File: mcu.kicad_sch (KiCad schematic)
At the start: 7 parts

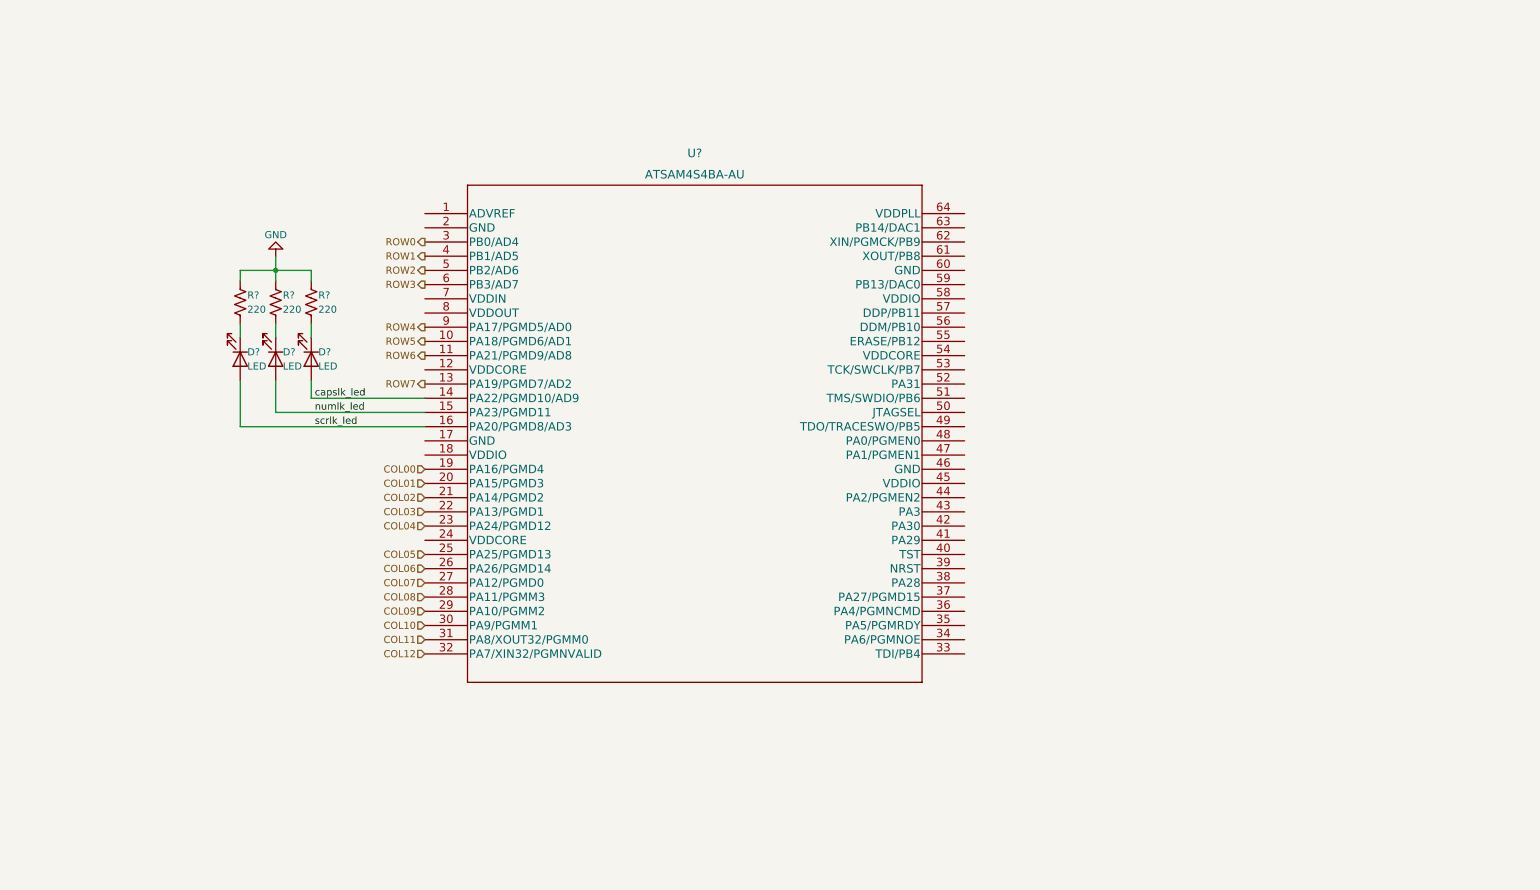
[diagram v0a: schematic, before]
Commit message: Add USB connector and rotary encoder
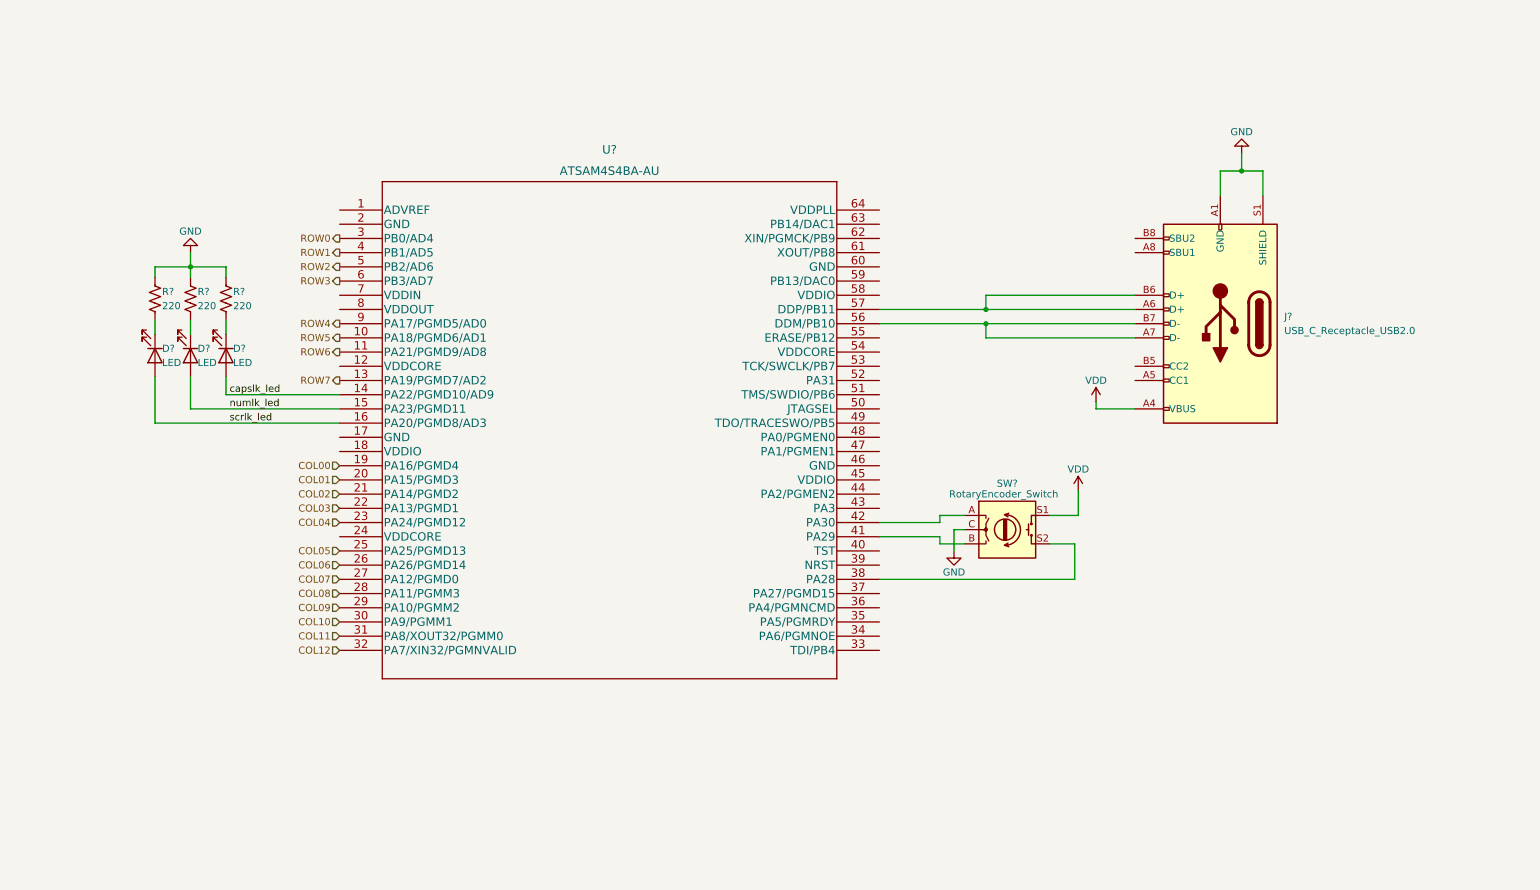
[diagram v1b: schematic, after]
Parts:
- added J?: USB_C_Receptacle_USB2.0, symbol Connector:USB_C_Receptacle_USB2.0
- added SW?: RotaryEncoder_Switch, symbol Device:RotaryEncoder_Switch
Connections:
- net GND: now also J?.A1 (GND), J?.A12 (GND), J?.B1 (GND), J?.B12 (GND), J?.S1 (SHIELD), SW?.C
- net at U?.38 (PA28): now also SW?.S2
- net at U?.41 (PA29): now also SW?.B
- net at U?.42 (PA30): now also SW?.A
- net at U?.56 (DDM/PB10): now also J?.A7 (D-), J?.B7 (D-)
- net at U?.57 (DDP/PB11): now also J?.A6 (D+), J?.B6 (D+)
- new net VDD: J?.A4 (VBUS), J?.A9 (VBUS), J?.B4 (VBUS), J?.B9 (VBUS), SW?.S1
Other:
- moved on the sheet: D?, R?, U?

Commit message: Add vol switches
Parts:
- removed J?: USB_C_Receptacle_USB2.0, symbol Connector:USB_C_Receptacle_USB2.0
- removed SW?: RotaryEncoder_Switch, symbol Device:RotaryEncoder_Switch
- added C?: 2.2u, symbol Device:C
- added C? (x2): 1u, symbol Device:C
- added C? (x2): 22p, symbol Device:C
- added C?: 100n, symbol Device:C
- added C?: 4.7u, symbol Device:C
- added J?: USB_C_Receptacle_USB2.0, symbol Connector:USB_C_Receptacle_USB2.0
- added R? (x2): 56K, symbol Device:R_US
- added R? (x3): 10K, symbol Device:R_US
- added R? (x2): 27, symbol Device:R_US
- added SW? (x3): SW_DIP_x01, symbol Switch:SW_DIP_x01
- added SW?: RotaryEncoder, symbol Device:RotaryEncoder
- added U?: TLV1117LV, symbol LDOs:TLV1117LV
- added Y?: XTAL-12M, symbol Device:Crystal
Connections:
- net GND: now also U?.17 (GND), U?.2 (GND), U?.46 (GND), U?.60 (GND), C?.2, C?.2, C?.2, C?.2, C?.2, C?.2, C?.2, J?.A1 (GND), J?.A12 (GND), J?.B1 (GND), J?.B12 (GND), J?.S1 (SHIELD), R?.1, R?.1, R?.1, R?.1, R?.1, SW?.C, U?.1 (Gnd)
- net VDD: now also U?.1 (ADVREF), U?.18 (VDDIO), U?.45 (VDDIO), U?.58 (VDDIO), U?.7 (VDDIN), C?.1, C?.1, SW?.2, SW?.2, SW?.2, U?.2 (Vout)
- net at U?.42 (PA30): now also SW?.A
- net at U?.41 (PA29): now also SW?.B
- net vol+: now reaches U?.38 (PA28)
- net vol+: now also R?.2, SW?.1
- net vdd_int_reg: now reaches U?.12 (VDDCORE)
- net vdd_int_reg: now also U?.24 (VDDCORE), U?.54 (VDDCORE), U?.64 (VDDPLL), U?.8 (VDDOUT), C?.1, C?.1
- net volm: now reaches U?.36 (PA4/PGMNCMD)
- net volm: now also R?.2, SW?.1
- net vol-: now reaches U?.37 (PA27/PGMD15)
- net vol-: now also R?.2, SW?.1
- net at U?.56 (DDM/PB10): now also R?.1
- net at U?.57 (DDP/PB11): now also R?.1
- net at U?.61 (XOUT/PB8): now also C?.1, Y?.1
- net at U?.62 (XIN/PGMCK/PB9): now also C?.1, Y?.2
- new net: J?.A5 (CC1), R?.2
- new net: J?.B5 (CC2), R?.2
- new net: J?.A6 (D+), J?.B6 (D+), R?.2
- new net: J?.A7 (D-), J?.B7 (D-), R?.2
- new net VBUS: C?.1, J?.A4 (VBUS), J?.A9 (VBUS), J?.B4 (VBUS), J?.B9 (VBUS), U?.3 (Vin)
- no-connect marks 0 -> 2
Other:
- note added: "A 4.7µF or higher ceramic capacitor must be connected between VDDIN and the closest GND pin of the device. This large decoupling capacitor is mandatory to reduce startup current, improving transient response and noise rejection."
- note added: "To ensure stability, an external 2.2 µF output capacitor, CDOUT must be connected between the VDDOUT and the closest GND pin of the device. The ESR of the capacitor must be in the range 0.1 to 10 Ω. Solid tantalum, and multilayer ceramic capacitors are all suitable as output capacitor. A 100 nF bypass capacitor between VDDOUT and the closest GND pin of the device helps decrease output noise and i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"
- moved on the sheet: D?, R?, U?

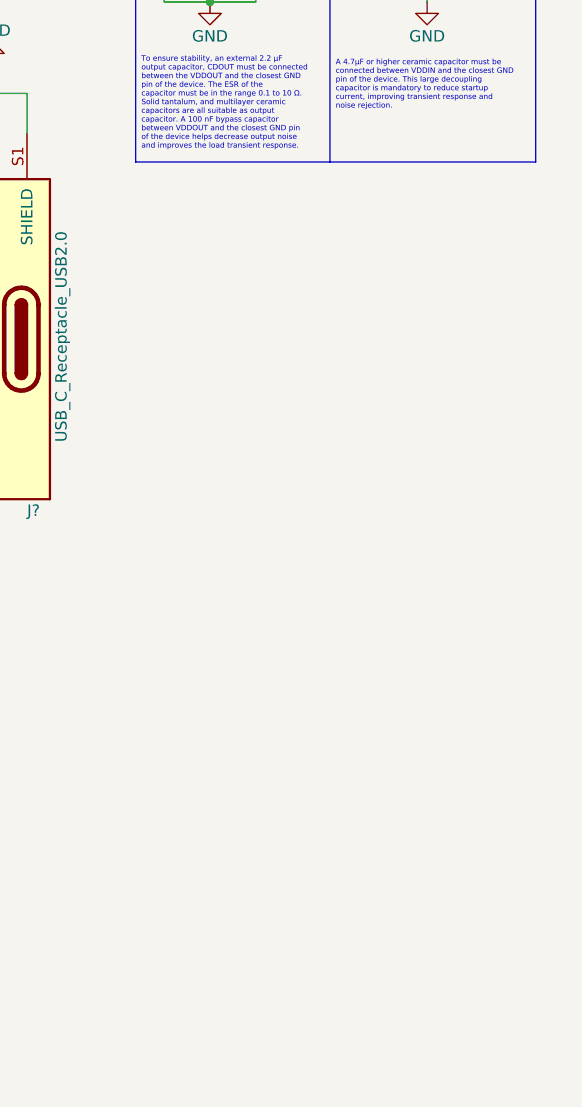
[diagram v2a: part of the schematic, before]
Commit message: Add pulldown resistors to column pins
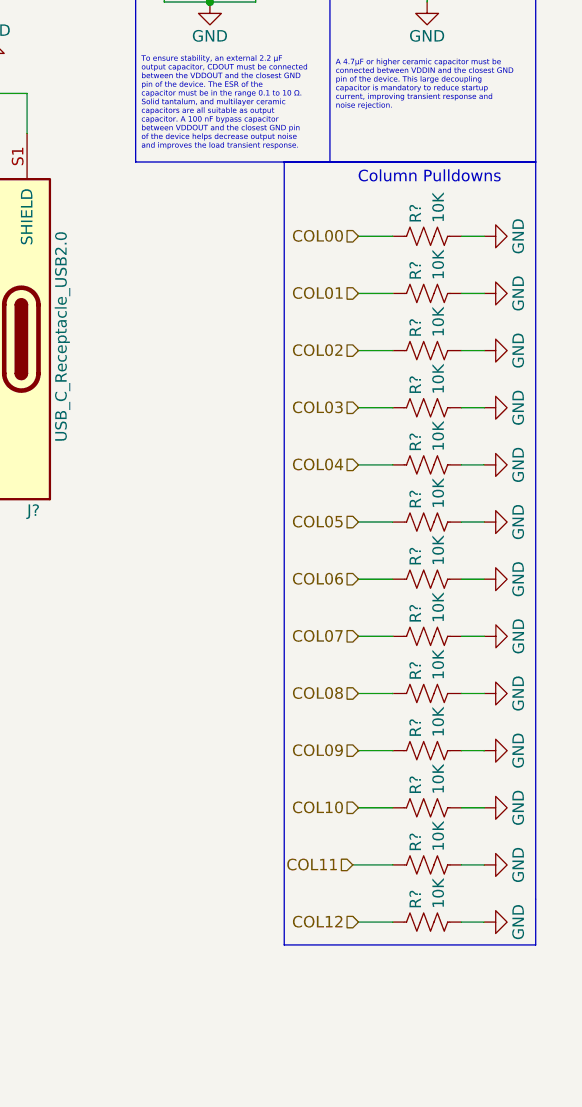
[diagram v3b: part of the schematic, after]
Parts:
- added R? (x13): 10K, symbol Device:R_US
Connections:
- net COL00: now also R?.1
- net COL01: now also R?.1
- net COL02: now also R?.1
- net COL03: now also R?.1
- net COL04: now also R?.1
- net COL05: now also R?.1
- net COL06: now also R?.1
- net COL07: now also R?.1
- net COL08: now also R?.1
- net COL09: now also R?.1
- net COL10: now also R?.1
- net COL11: now also R?.1
- net COL12: now also R?.1
- net GND: now also R?.2, R?.2, R?.2, R?.2, R?.2, R?.2, R?.2, R?.2, R?.2, R?.2, R?.2, R?.2
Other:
- note added: "Column Pulldowns"

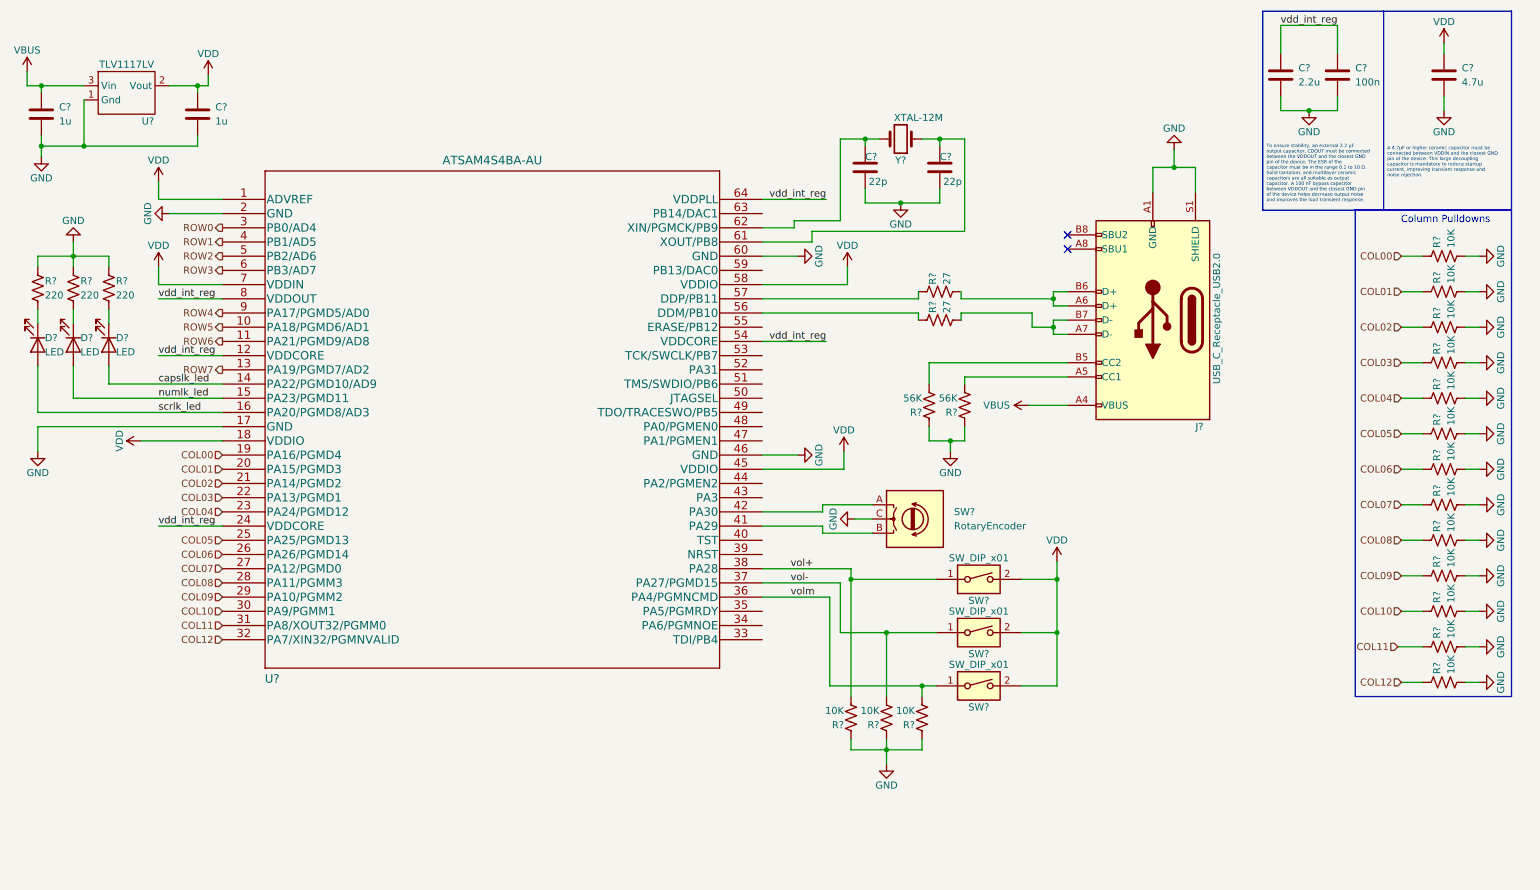
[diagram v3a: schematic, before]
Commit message: Add RGB LEDs, assign footpritns, begin placement
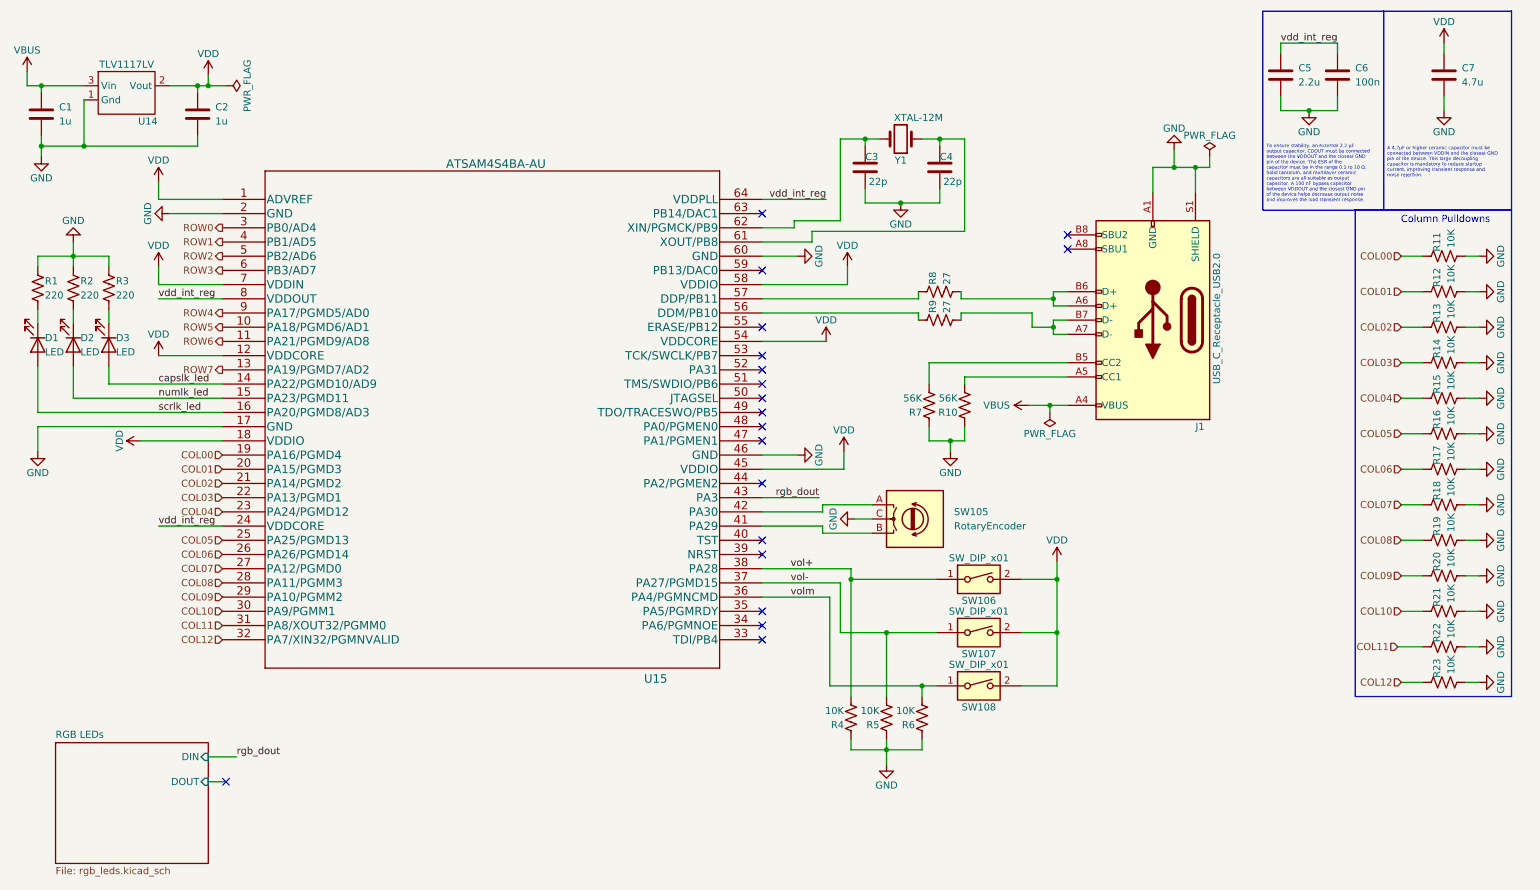
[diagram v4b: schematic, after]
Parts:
- C1, C2, C3, C4, C5, C6, C7: renamed from C?; footprint (none) -> Capacitor_SMD:C_0805_2012Metric_Pad1.18x1.45mm_HandSolder
- D1, D2, D3: renamed from D?; footprint (none) -> LED_SMD:LED_0805_2012Metric_Pad1.15x1.40mm_HandSolder
- J1: renamed from J?; footprint (none) -> Connector_USB:USB_C_Receptacle_GCT_USB4105-xx-A_16P_TopMnt_Horizontal
- R1, R10, R11, R12, R13, R14, R15, R16, R17, R18, R19, R2, R20, R21, R22, R23, R3, R4, R5, R6, R7, R8, R9: renamed from R?; footprint (none) -> Resistor_SMD:R_0805_2012Metric_Pad1.20x1.40mm_HandSolder
- SW105: renamed from SW?; footprint (none) -> Rotary_Encoder:RotaryEncoder_Bourns_Vertical_PEC12R-3xxxF-Sxxxx
- SW106, SW107, SW108: renamed from SW?; footprint (none) -> keyswitches:Kailh_socket_MX_optional_reversible
- U14: renamed from U?; footprint (none) -> Package_TO_SOT_SMD:SOT-223-3_TabPin2
- U15: renamed from U?; footprint QFP64-10x10MC_MCH -> Package_QFP:LQFP-64_10x10mm_P0.5mm
- Y1: renamed from Y?; footprint (none) -> Crystal:Crystal_SMD_HC49-SD_HandSoldering
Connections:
- net GND: now also R18.2
- net VDD: now also U15.12 (VDDCORE), U15.54 (VDDCORE)
- net vdd_int_reg: no longer U15.12 (VDDCORE), U15.54 (VDDCORE)
- net rgb_dout: now reaches U15.43 (PA3)
- no-connect marks 2 -> 19
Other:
- added sheet RGB LEDs (rgb_leds.kicad_sch)

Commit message: Place all switches
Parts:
- U15: footprint Package_QFP:LQFP-64_10x10mm_P0.5mm -> QFP64-10x10MC_MCH
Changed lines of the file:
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@@
       (effects (font (size 1.524 1.524)))
     )
-    (property "Footprint" "Package_QFP:LQFP-64_10x10mm_P0.5mm" (id 2) (at 101.6 40.259 0)
+    (property "Footprint" "QFP64-10x10MC_MCH" (id 2) (at 101.6 40.259 0)
       (effects (font (size 1.524 1.524)) hide)
     )

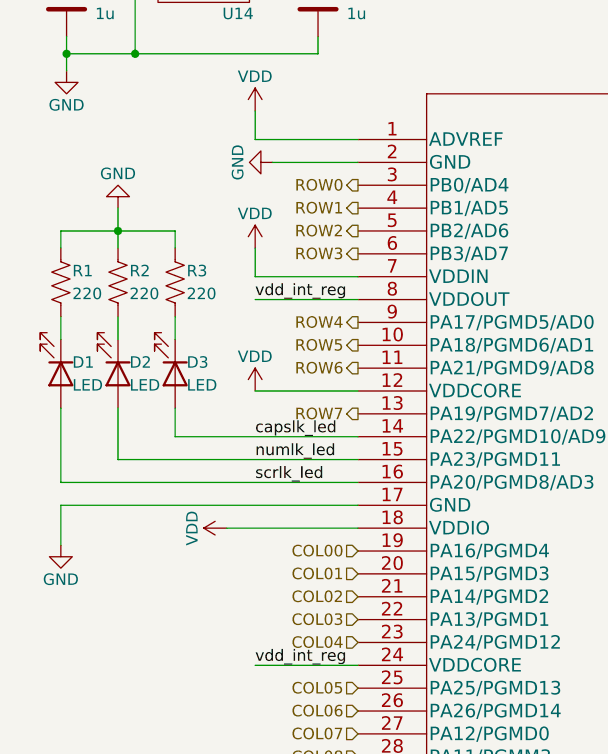
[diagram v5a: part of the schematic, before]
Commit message: Roughly place LEDs. Add decoupling caps to schematic for LEDs.
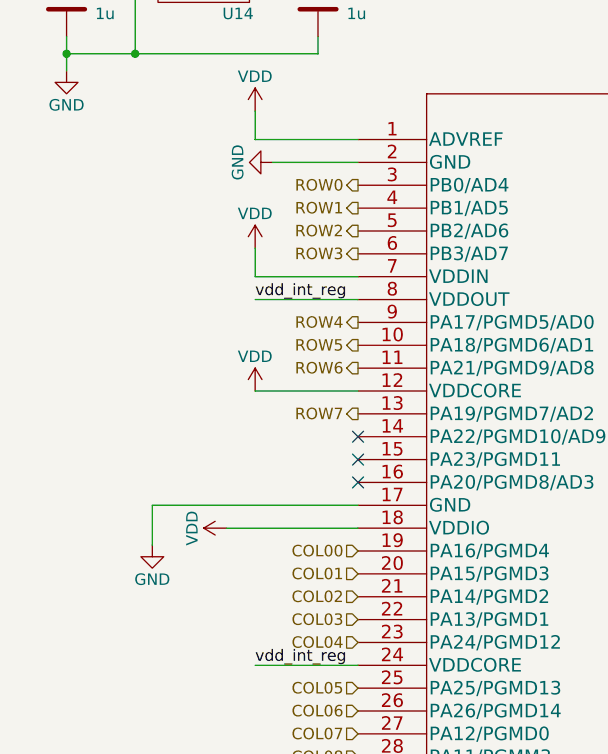
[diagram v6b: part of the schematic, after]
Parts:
- removed D1, D2, D3: LED, LED_SMD:LED_0805_2012Metric_Pad1.15x1.40mm_HandSolder, symbol Device:LED
- removed R1, R2, R3: 220, Resistor_SMD:R_0805_2012Metric_Pad1.20x1.40mm_HandSolder, symbol Device:R_US
- SW106, SW107, SW108: footprint keyswitches:Kailh_socket_MX_optional_reversible -> Switch_Keyboard_Hotswap_Kailh:SW_Hotswap_Kailh_MX
- U15: footprint QFP64-10x10MC_MCH -> Package_QFP:TQFP-64_10x10mm_P0.5mm
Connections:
- net capslk_led: no longer names the net of U15.14 (PA22/PGMD10/AD9)
- net numlk_led: no longer names the net of U15.15 (PA23/PGMD11)
- net scrlk_led: no longer names the net of U15.16 (PA20/PGMD8/AD3)
- no-connect marks 19 -> 22
